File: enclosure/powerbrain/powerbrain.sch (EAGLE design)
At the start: 42 parts, among them J3 AVR_SPI_PRG_6PTH, Q1 FDD4141TO252, Q2 200mA/50V, U2 TPS61090, X2 ZX62D-B-5PA8

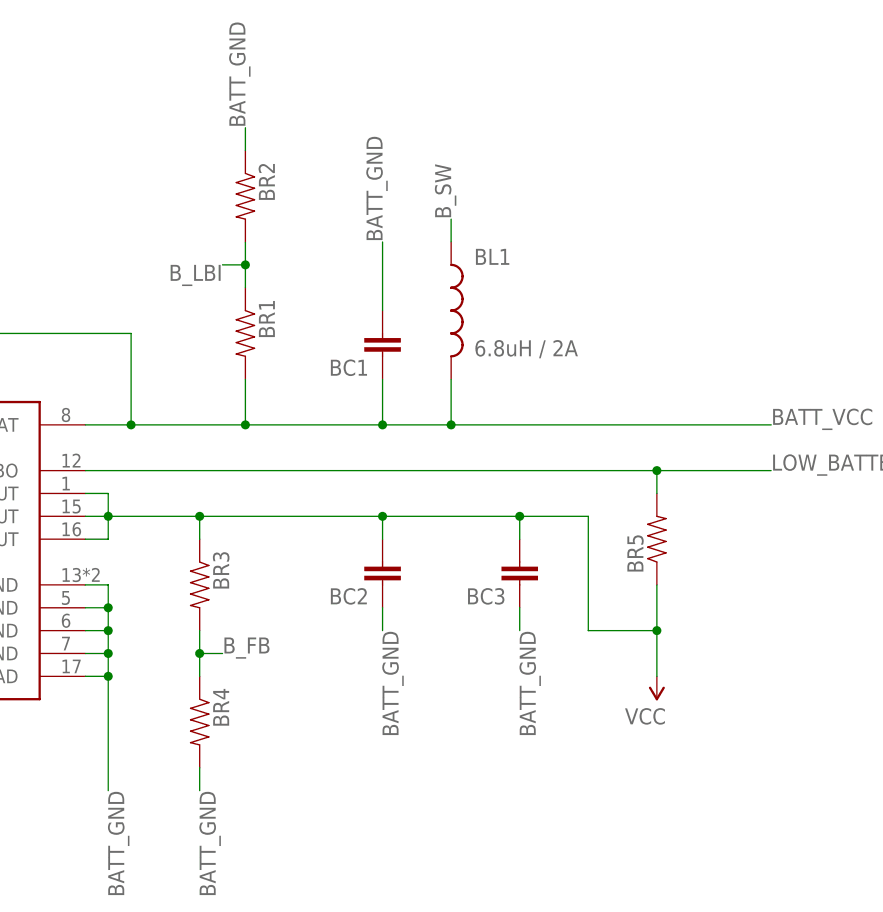
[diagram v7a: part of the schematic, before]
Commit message: powerbrain: resistor/capacitor values for boost converter
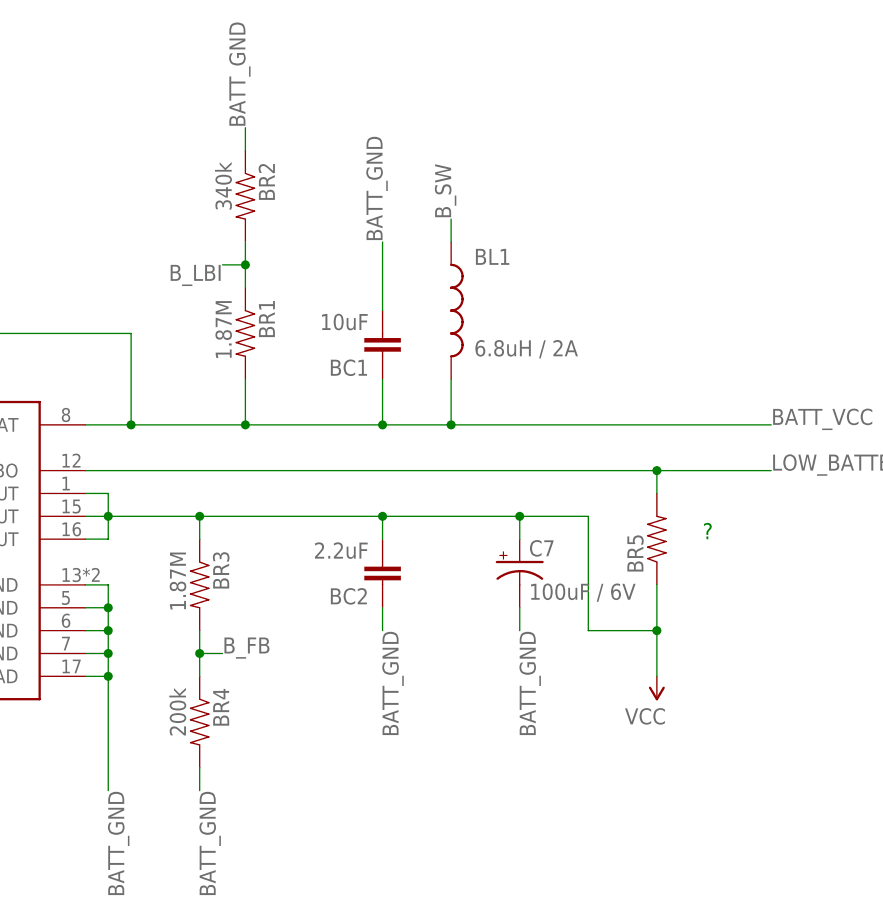
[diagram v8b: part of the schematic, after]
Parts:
- removed BC3: (no value), SparkFun-Capacitors:CAP1206
- added C7: 100uF / 6V, SparkFun-Passives:CAP_POL3528-KIT
- BC1: value (none) -> 10uF
- BC2: value (none) -> 2.2uF
- BL1: device SparkFun-Passives:INDUCTORNPI75 -> SparkFun-Passives:INDUCTOR-B82462G
- BR1, BR3: value (none) -> 1.87M
- BR2: value (none) -> 340k
- BR4: value (none) -> 200k
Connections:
- net BATT_GND: now also C7.-; no longer BC3.1
- net VCC: now also C7.+; no longer BC3.2
